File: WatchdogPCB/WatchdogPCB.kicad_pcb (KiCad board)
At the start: 4 copper layers, 120 x 50 mm, 35 parts, among them J1 Roll hoop, J2 Speed & Oil, J3 H bridge driver control, J4 Power, J5 Thermistor 1, J6 Thermistor 2, J7 Dashboard A, J8 Dashboard B, U2 MCP602, U3 DS3695N

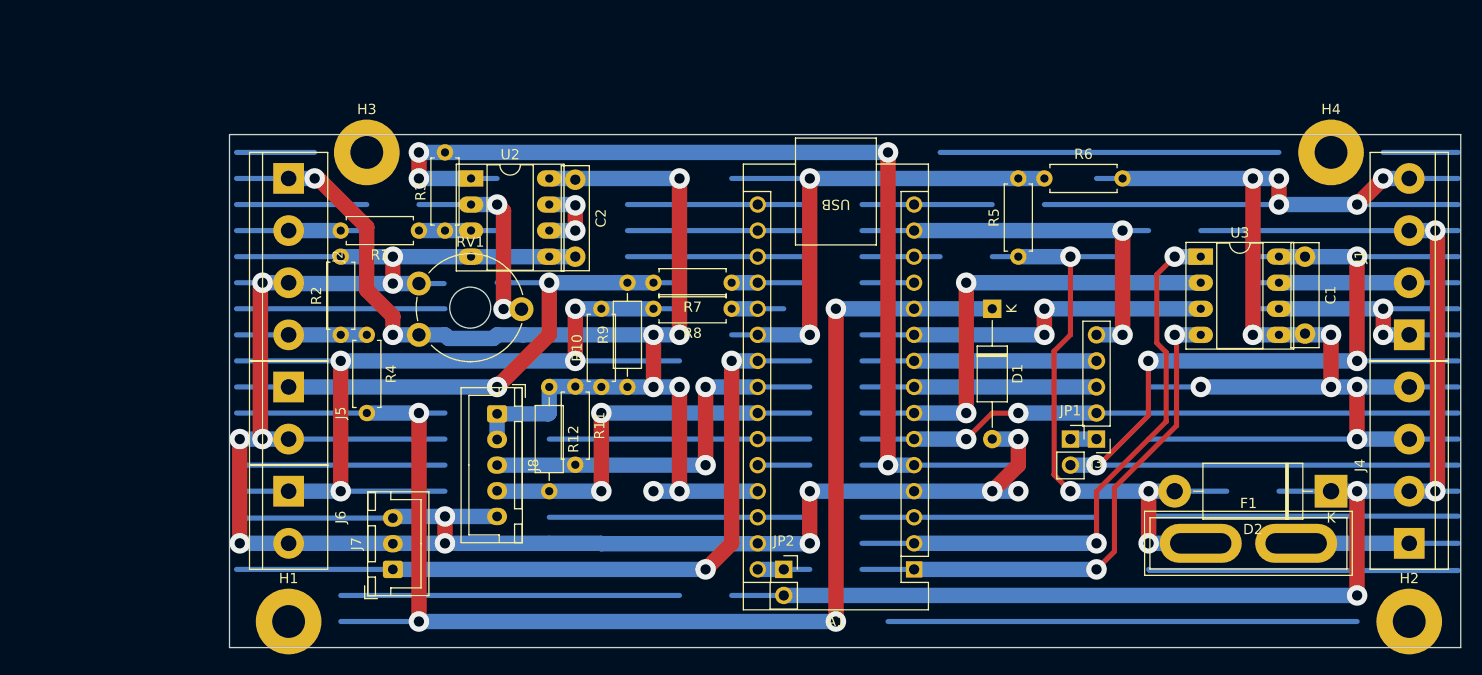
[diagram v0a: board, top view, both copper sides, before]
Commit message: Adding pinout to PCB and tidying up CAD
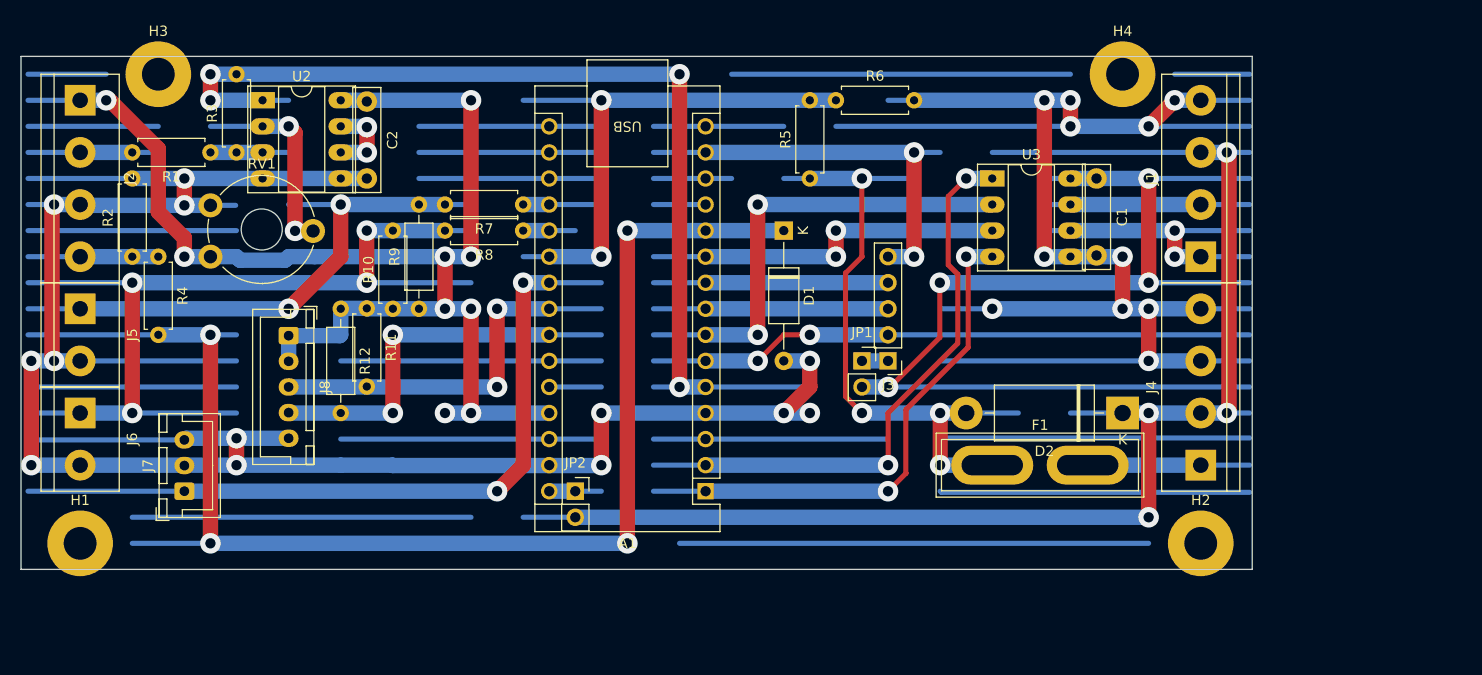
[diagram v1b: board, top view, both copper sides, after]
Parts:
- moved D2 21.7 mm to (193.0, 104.1)
- moved JP1 21.7 mm to (167.6, 99.1)
- moved H4 21.7 mm to (193.0, 71.1)
- moved JP2 21.7 mm to (139.7, 111.8)
- moved H1 21.7 mm to (91.4, 116.8)
- moved J2 21.7 mm to (91.4, 73.7)
- moved J5 21.7 mm to (91.4, 94.0)
- moved J6 21.7 mm to (91.4, 104.1)
- moved J7 21.7 mm to (101.6, 111.8)
- moved J8 21.7 mm to (111.8, 96.6)
- moved R10 21.7 mm to (121.9, 94.0)
- moved R2 21.7 mm to (96.5, 88.9)
- moved R9 21.7 mm to (124.5, 94.0)
- moved C1 21.7 mm to (190.5, 81.3)
- moved C2 21.7 mm to (119.4, 73.8)
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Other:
- board text added: "+Ignition"
- board text added: "-Ignition"
- board text added: "5V"
- board text added: "Aux."
- board text added: "Horn"
- board text added: "Motor A"
- board text added: "Motor B"
- board text added: "Motor GND"
- board text added: "Motor power"
- board text added: "Oil pressure"
- board text added: "Remote +RS485"
- board text added: "Remote -RS485"
- board text added: "Remote GND"
- board text added: "Remote power"
- board text added: "Tach. 5V"
- board text added: "Tach. GND"
- board text added: "Tach. signal"
- board text added: "Thermistor 1"
- board text added: "Thermistor 2"
- board text added: "Thermistor GND"

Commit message: Schematics modified to use pages for wiring diagram, remote unit started, working on enclosure.
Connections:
- net /Aux renamed /Main PCB/Aux
- net /Button renamed /Main PCB/Dash. BTN
- net /Hall effect renamed /Main PCB/Tach. hall
- net /Horn renamed /Main PCB/Horn
- net /Motor A renamed /Main PCB/Motor A
- net /Motor B renamed /Main PCB/Motor B
- net /Oil renamed /Main PCB/Oil SW
- net /Power in renamed +VDC
- net /SCL renamed /Main PCB/Dash. SCL
- net /SDA renamed /Main PCB/Dash. SDA
- net /Threshold adjust renamed /Main PCB/Threshold adjust
- net Net-(J1-Pin_1) renamed /Main PCB/+RS485
- net Net-(J1-Pin_2) renamed /Main PCB/-RS485
- net Net-(J3-Pin_1) renamed /Main PCB/Motor driver 5V
- net Net-(J5-Pin_1) renamed /Main PCB/Thermistor 1
- net Net-(J6-Pin_1) renamed /Main PCB/Thermistor 2
